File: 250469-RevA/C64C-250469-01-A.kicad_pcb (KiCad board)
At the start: 2 copper layers, 390 x 135.9 mm, 132 parts, among them J1 Conn_01x20_Male, J10 LED, J2 Conn_02x12_Edge, J3 Conn_02x6_Edge, J4 DIN-6, J5 DIN-8, J6 Conn_02x22_Edge_Female, J7 DIN-7, J8 DB9_Female, J9 DB9_Female, M1 RF_Modulator, Q1 2SD313, Q2 2SC1815, Q3 2SC1815, Q5 2SC1384, U1 6526A, U10 41464, U11 41464, U18 4066, U19 2114, U2 6526A, U20 8701, U21 4066, U22 7416, U23 74LS14, U3 74LS08, U4 23128, U5 2332, U6 8500, U7 8565R2, U8 251715-01, U9 8580R5, Y1 Crystal

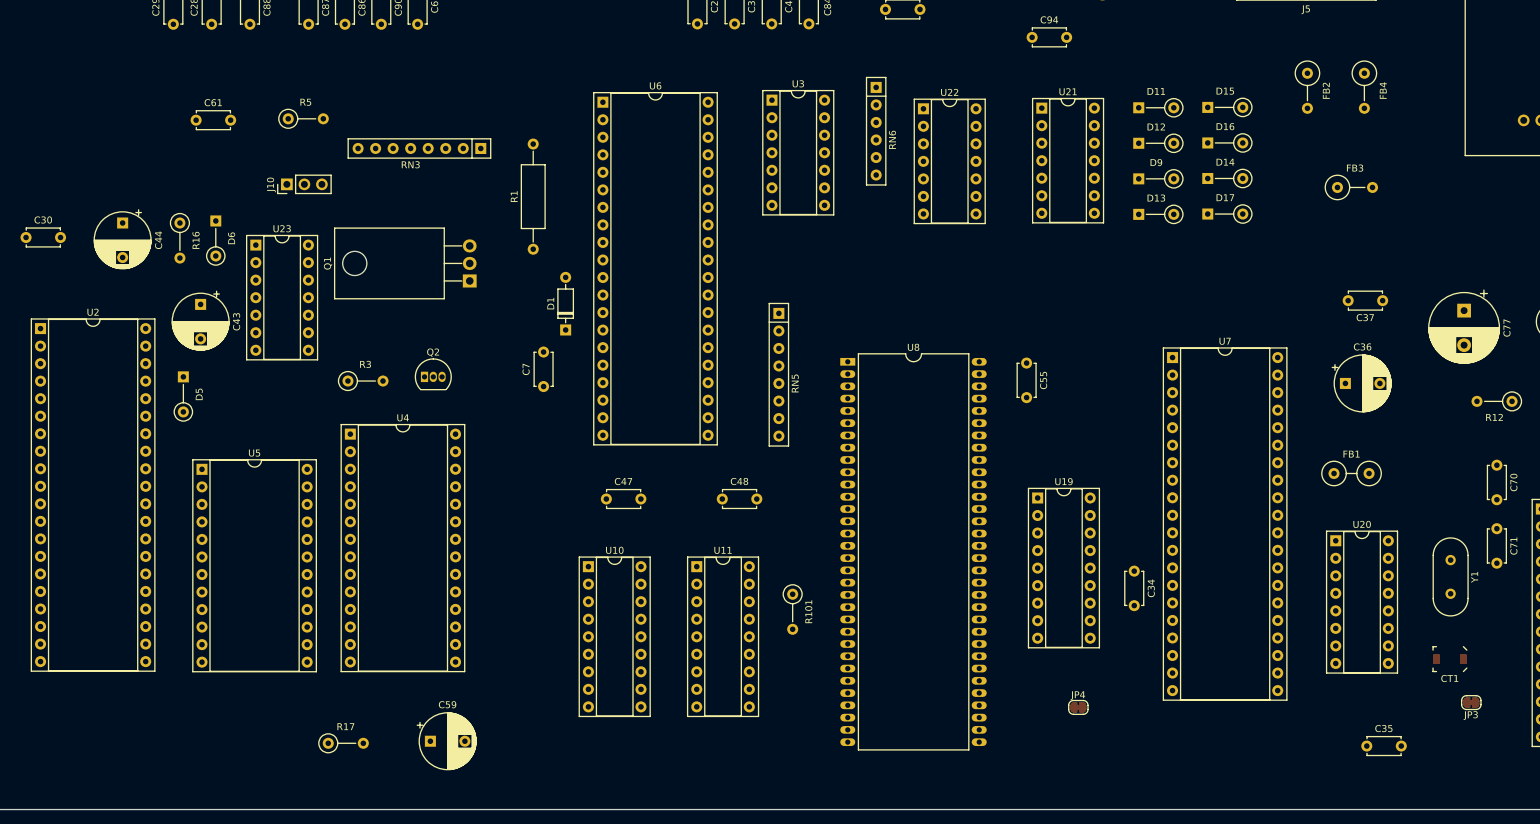
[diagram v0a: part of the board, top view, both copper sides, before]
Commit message: Add some artwork to the PCB
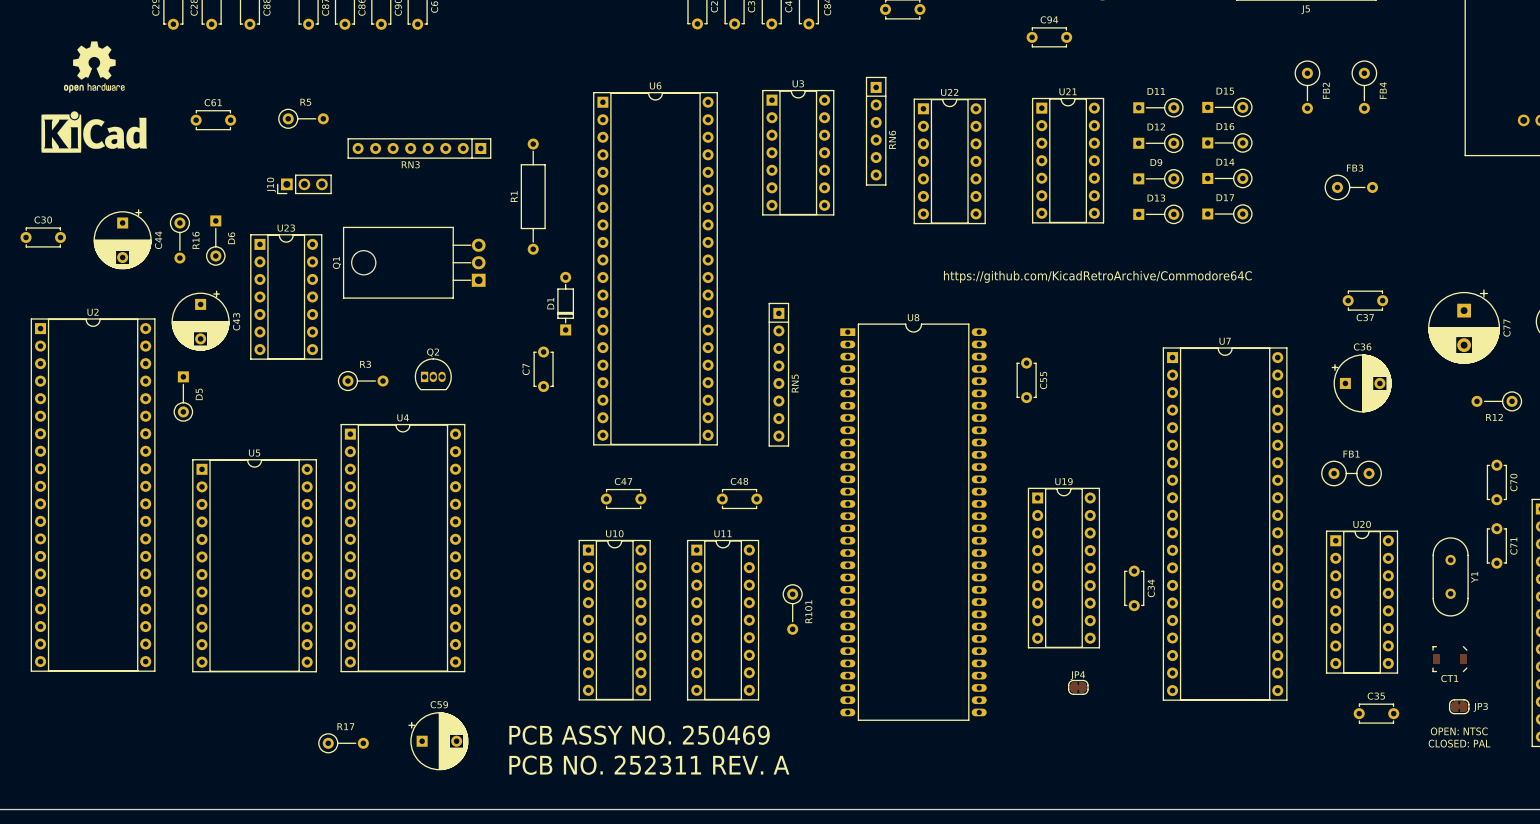
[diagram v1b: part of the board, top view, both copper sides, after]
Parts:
- added REF**: KiCad-Logo_6mm_SilkScreen, Symbol:KiCad-Logo_6mm_SilkScreen, F.Cu at (115.4, 167.3)
- added REF**: OSHW-Logo2_9.8x8mm_SilkScreen, Symbol:OSHW-Logo2_9.8x8mm_SilkScreen, F.Cu at (115.4, 157.9)
- moved C35 4.83 mm to (298.7, 251.6)
- moved U8 4.30 mm to (224.6, 196.3)
- moved JP4 2.90 mm to (258.0, 247.8)
- moved U10 2.40 mm to (187.0, 227.9)
- moved U11 2.40 mm to (202.7, 227.9)
- moved JP3 1.85 mm to (313.2, 250.6)
- moved Q1 1.30 mm to (171.1, 188.8)
- moved C59 1.20 mm to (162.9, 255.6)
- moved U23 0.61 mm to (139.4, 183.6)
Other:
- board text added: "OPEN: NTSC CLOSED: PAL"
- board text added: "PCB ASSY NO. 250469 PCB NO. 252311 REV. A"
- board text added: "https://github.com/KicadRetroArchive/Commodore64C"
